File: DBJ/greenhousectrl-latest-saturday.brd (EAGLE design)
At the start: 73.6 x 69.5 mm, 56 parts, among them IC1 ATMEGA168TQFP-08, IC4 L298, J1 POWER_JACKPTH, K2 G5LE, Q1 MMBT2222A, SW2 MOMENTARYBUTTON, U2 V_REG_317SMD, X1 CRYSTALS-NOGND-HC49

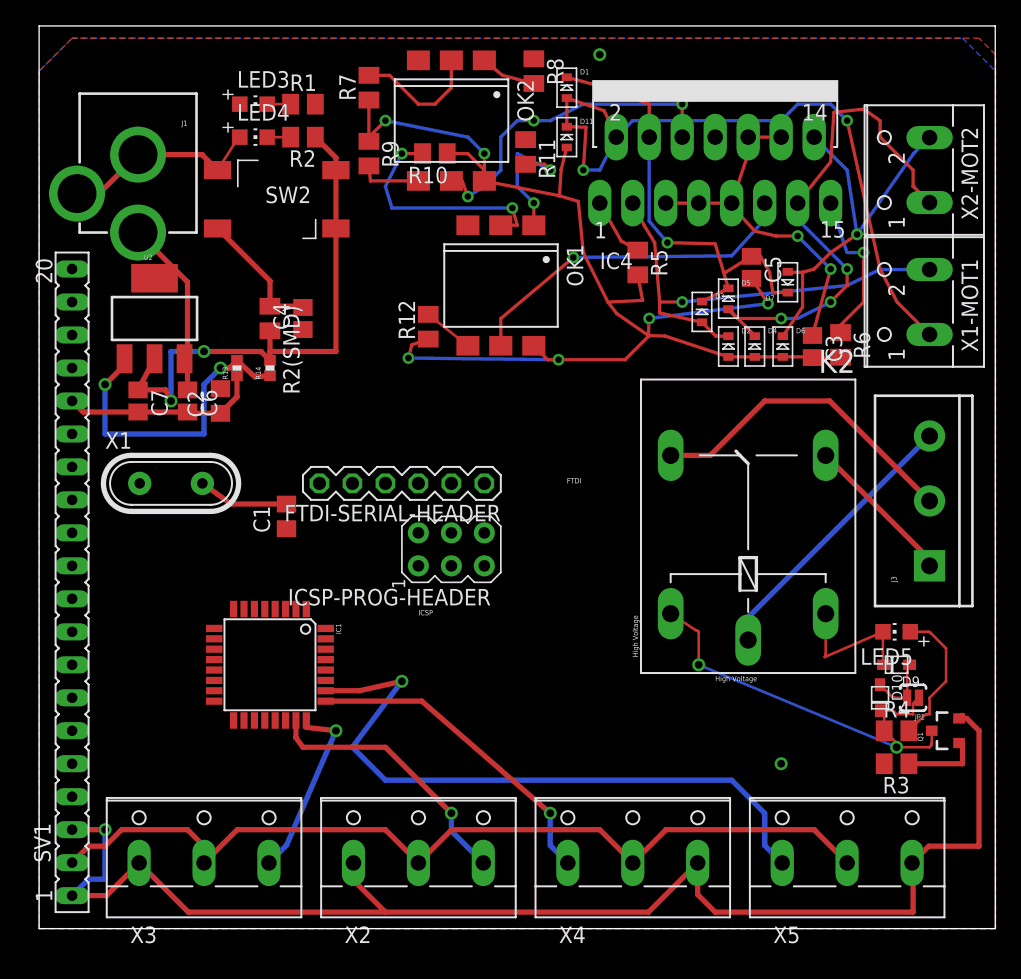
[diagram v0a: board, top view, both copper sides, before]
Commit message: erc and new vreg
ran erc on schematic, re-organized repository, used 7824DTvreg instead
of the vreg previously used due to erc giving errors
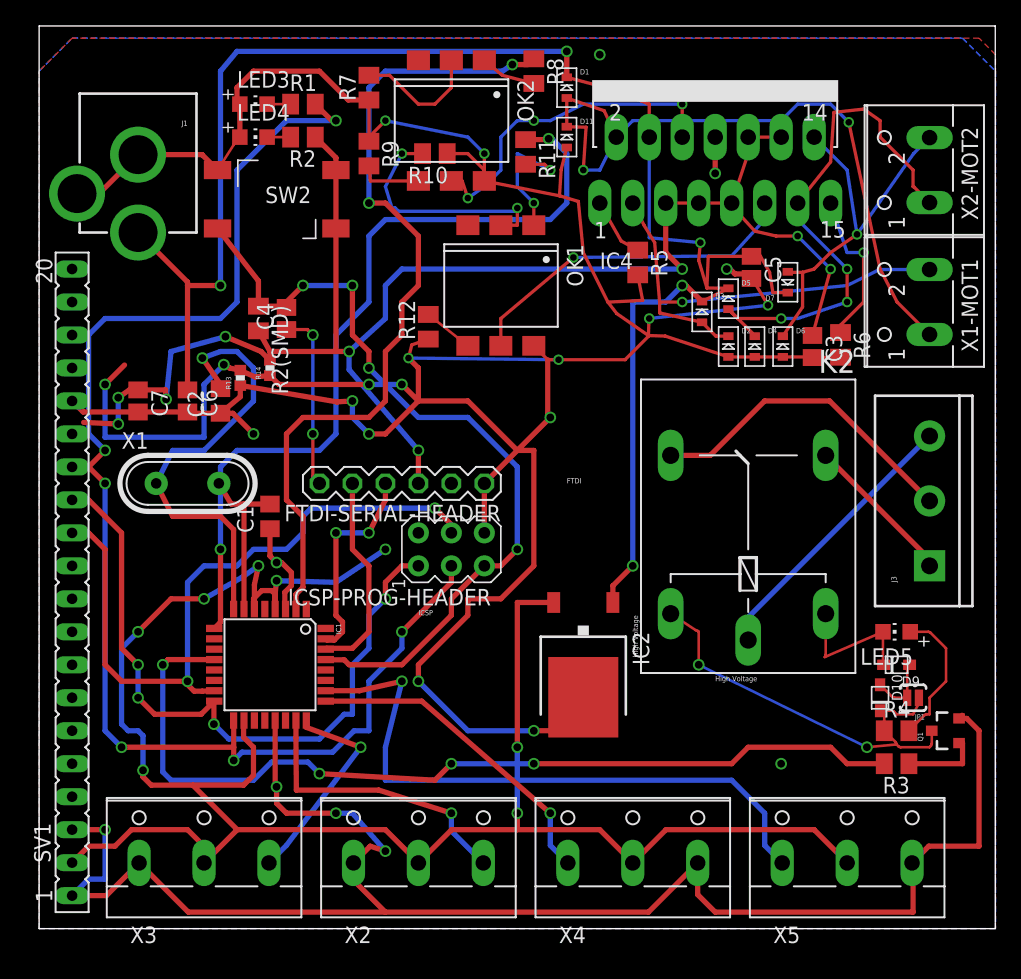
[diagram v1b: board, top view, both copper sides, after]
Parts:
- removed U2: V_REG_317SMD, SparkFun-PowerIC:SOT223
- added IC2: 7824DT, linear:TO252
- moved C1 1.27 mm to (17.8, 31.8)
- moved C4 1.27 mm to (19.1, 47.0)
- moved X1 1.27 mm to (11.4, 34.3)
- moved R2(SMD) 0.89 mm to (16.9, 47.0)
- moved R13 0.80 mm to (15.5, 42.4)
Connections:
- net +12V: now also IC2.1; no longer U2.3
- net +5V: now also IC2.2; no longer U2.2
- net N$7: now also IC2.3; no longer U2.1
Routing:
- net +5V: track 138.9 -> 272.7 mm, vias 4 -> 17
- net SCK: track 0.00 -> 107.5 mm, vias 0 -> 6
- net GND: track 236.7 -> 322.6 mm, vias 7 -> 17
- net +12V: track 48.8 -> 131.3 mm, vias 1 -> 5
- net PB0: track 0.00 -> 70.8 mm, vias 0 -> 4
- net PD4: track 0.00 -> 64.4 mm, vias 0 -> 2
- net PD5: track 0.00 -> 62.7 mm, vias 0 -> 2
- net N$7: track 24.2 -> 83.7 mm, vias 2 -> 6
- net MOSI: track 0.00 -> 53.6 mm, vias 0 -> 2
- net MISO: track 0.00 -> 52.9 mm, vias 0 -> 4
- net RST: track 10.2 -> 62.5 mm, vias 0 -> 4
- net N$13: track 0.00 -> 34.6 mm, vias 0 -> 1
- net TX: track 0.00 -> 16.1 mm, vias 0 -> 2
- net RX: track 0.00 -> 15.8 mm
- net DTR: track 0.00 -> 13.8 mm, vias 0 -> 2
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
